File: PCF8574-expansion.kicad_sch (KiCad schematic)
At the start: 20 parts, among them J11 LED_1, J11 Power, J12 LED_2, J13 LED_3, J14 LED_4, J32 I2C, U3 PCF8574

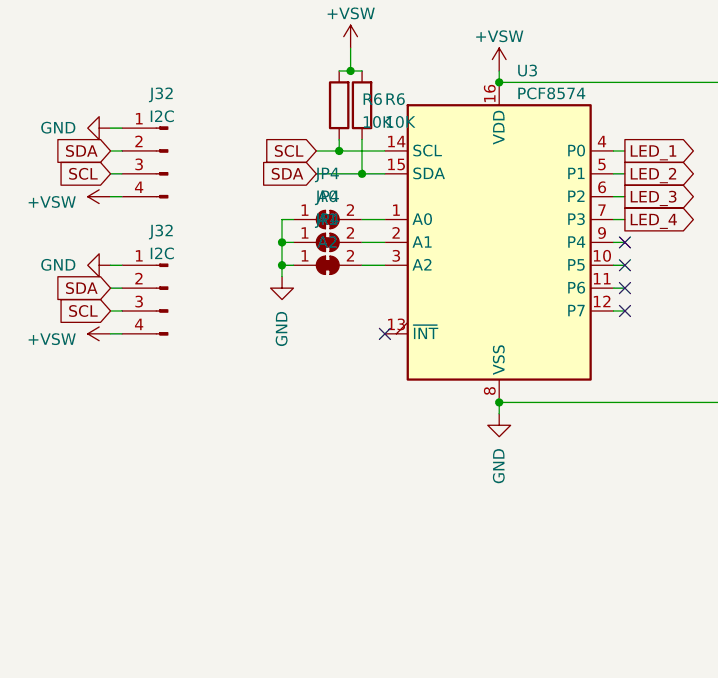
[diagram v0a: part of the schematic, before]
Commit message: Added adress pullups
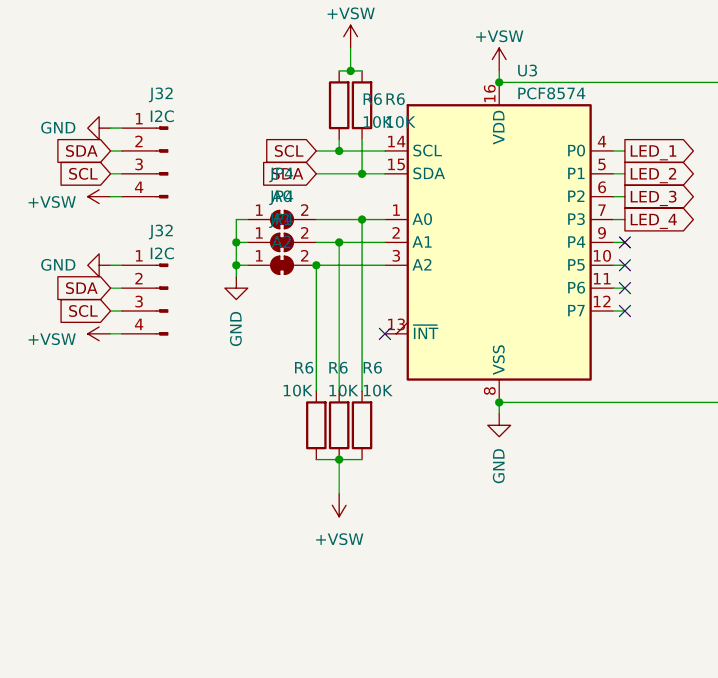
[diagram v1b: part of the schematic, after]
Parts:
- added R6 (x3): 10K, Resistor_SMD:R_0805_2012Metric_Pad1.20x1.40mm_HandSolder, symbol Device:R
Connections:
- net +VSW: now also R6.1, R6.1, R6.1
- net at JP4.2 (B), U3.2 (A1): now also R6.2
- net at JP4.2 (B), U3.1 (A0): now also R6.2
- net at JP4.2 (B), U3.3 (A2): now also R6.2
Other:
- moved on the sheet: JP4
